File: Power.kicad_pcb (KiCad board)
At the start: 6 copper layers, 53 x 108.8 mm, 298 parts, among them Y1 16M

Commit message: WIP разводка: C_gs нижних ключей (C102/C103, C106/C107, C110/C111)
Нижние C_gs — под R_g нижнего ряда, GND у C107/C111 своими виа (полоса GND
там уже закончилась). Верхние — в полосе GND у R_gs/R_g; под них в полосе
сдвинуты 3/3/2 виа истоков внутри той же полосы: число виа полос 92/37/33,
как в rev0 (Р8). DRC: 0 ошибок.

Co-Authored-By: Claude Opus 5.5 <noreply@anthropic.com>
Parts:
- moved C110 56.5 mm to (151.5, 81.4), turned to -90 degrees
- moved C111 56.5 mm to (153.4, 90.5), turned to -90 degrees
- moved C107 39.8 mm to (136.9, 90.2), turned to -90 degrees
- moved C102 38.4 mm to (120.0, 82.7), turned to 180 degrees
- moved C106 37.7 mm to (135.0, 80.5)
- moved C103 36.0 mm to (120.0, 91.4), turned to 180 degrees
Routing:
- net GND: track 238.8 -> 240.6 mm, vias 231 -> 233
- net Net-(C106-Pad1): track 3.15 -> 4.99 mm
- net Net-(C110-Pad1): track 3.40 -> 5.09 mm
- net Net-(C102-Pad1): track 3.64 -> 5.14 mm
- net Net-(C107-Pad1): track 3.76 -> 5.26 mm
- net Net-(C103-Pad1): track 3.40 -> 4.87 mm
- net Net-(C111-Pad1): track 3.36 -> 4.53 mm

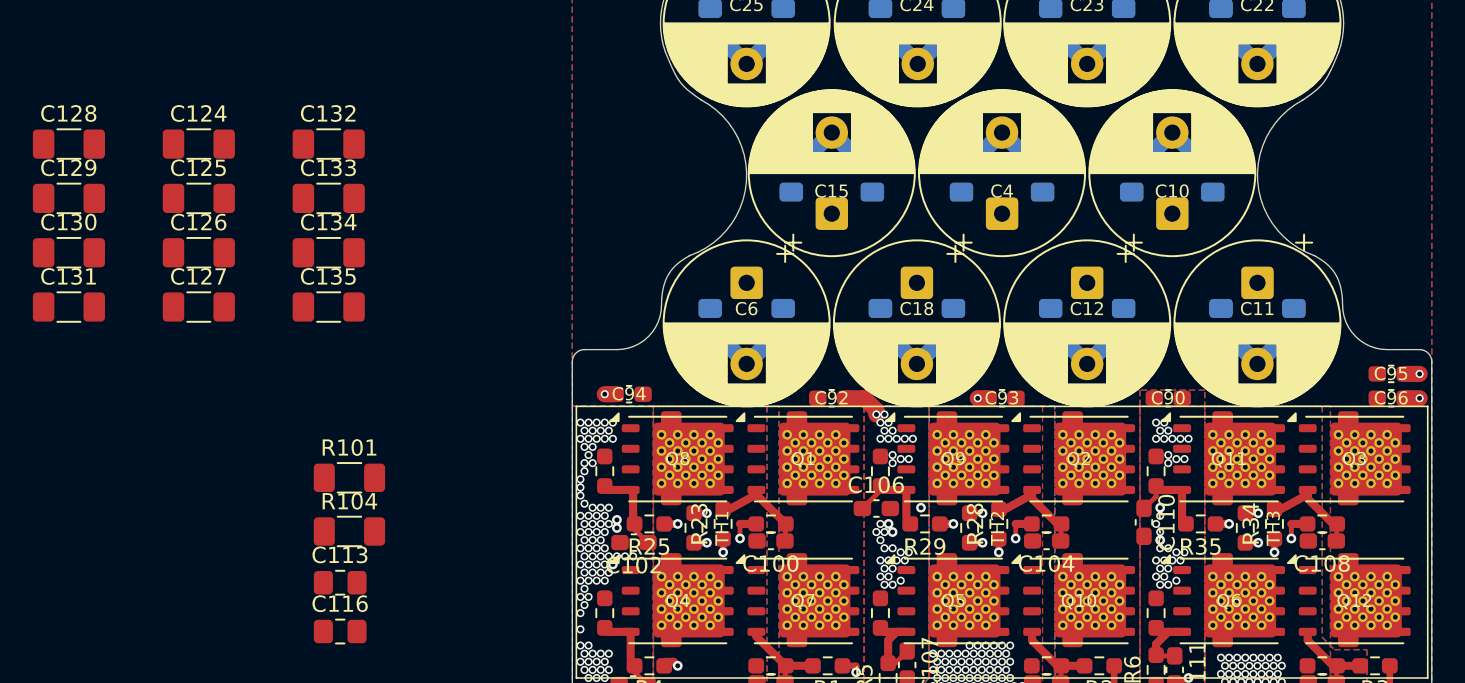
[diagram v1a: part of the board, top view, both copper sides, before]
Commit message: WIP разводка: керамика §4 — по одному 1206 на фазу; лишние три на фазу убраны из схемы
1206 1u 100V (C124/C128/C132) в среднем ряду колонки стока HS, одинаково на
трёх фазах, у каждого своя пара виа (VDC и GND). Верхняя полоса над стоком
занята корпусами банок ЗПТ Ø10 (по футпринту до y 74.1), нижний ряд — R_g
нижнего HS; поэтому C125–C127, C129–C131, C133–C135 удалены из схемы и платы
(Р6, «по месту»). C110 переставлен вглубь полосы A (4 виа сдвинуты в полосе).
DRC: 0 ошибок, расхождений со схемой нет; ERC: 9 (база).

Co-Authored-By: Claude Opus 5.5 <noreply@anthropic.com>
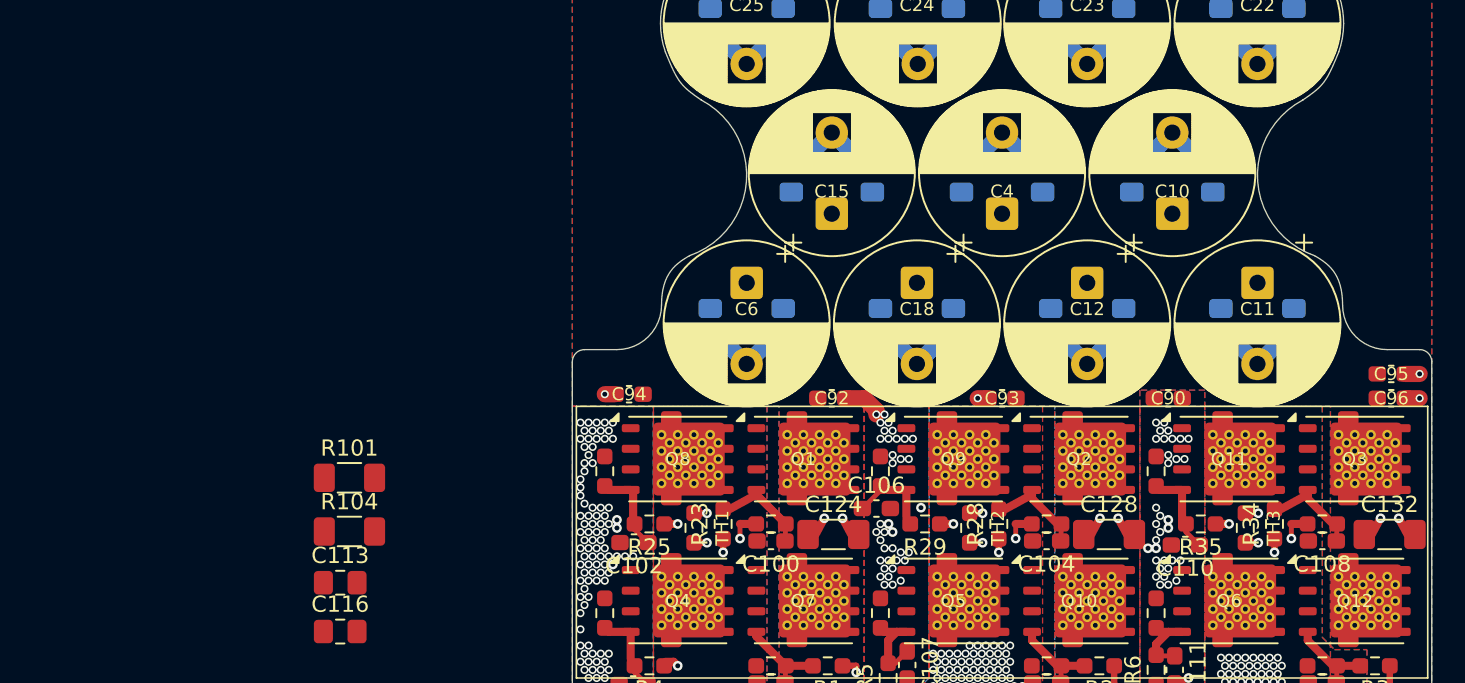
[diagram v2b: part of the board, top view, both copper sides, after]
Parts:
- removed C125, C126, C127, C129, C130, C131, C133, C134, C135: 1u 100V X7R, Capacitor_SMD:C_1206_3216Metric_Pad1.33x1.80mm_HandSolder
- moved C132 69.7 mm to (166.7, 82.2)
- moved C128 68.5 mm to (149.3, 82.2)
- moved C124 45.9 mm to (132.3, 82.2)
- moved C110 2.91 mm to (154.1, 82.8), turned to 180 degrees
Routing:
- net GND: track 240.6 -> 244.0 mm, vias 233 -> 236
- net VDC: track 30.5 -> 33.9 mm, vias 0 -> 3
